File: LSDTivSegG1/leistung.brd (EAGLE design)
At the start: 150 x 100 mm, 87 parts, among them IC10 LM 2576 T15, IC11 LM 2576 T5.0, IC2 IR2184D, IC3 IR2184D, IC4 4081N, IC5 4069N, IC7 IR2184D, IC8 IR2184D, IC9 TINY13-20PU, Q1 IRFB3077, Q10 IRFB3077, Q11 IRFB3077, Q12 IRFB3077, Q2 IRFB3077, Q3 IRFB3077, Q4 IRFB3077, Q9 IRFB3077, X1 057-010-1, X2 MKDSN1,5/2-5,08

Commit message: added Text
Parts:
- F1, F2, F3: value (none) -> 1A
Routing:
- net GND: track 193.0 -> 181.2 mm
- net MOTOR_L_+: track 132.1 -> 123.8 mm
- net MOTOR_R_+: track 132.4 -> 130.8 mm
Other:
- board text added: "LSD-GR1-LST-D-T"
- board text added: "LSD-GR1-REG-D-+"
- board text added: "LSD-GR1-REG-D-BSTOP"
- board text added: "LSD-GR1-REG-D-TStop"

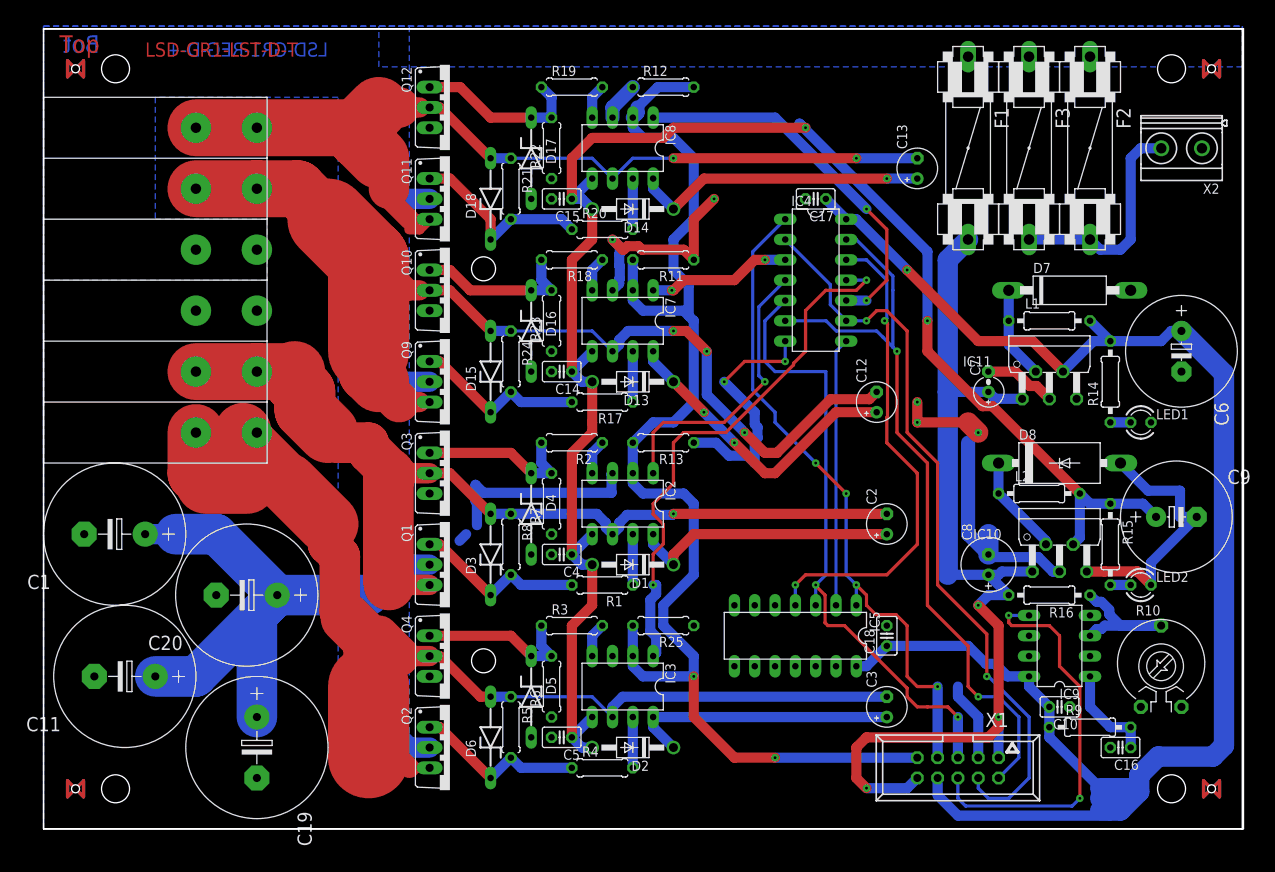
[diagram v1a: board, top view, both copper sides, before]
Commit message: fixes aus der Nachbesprechung
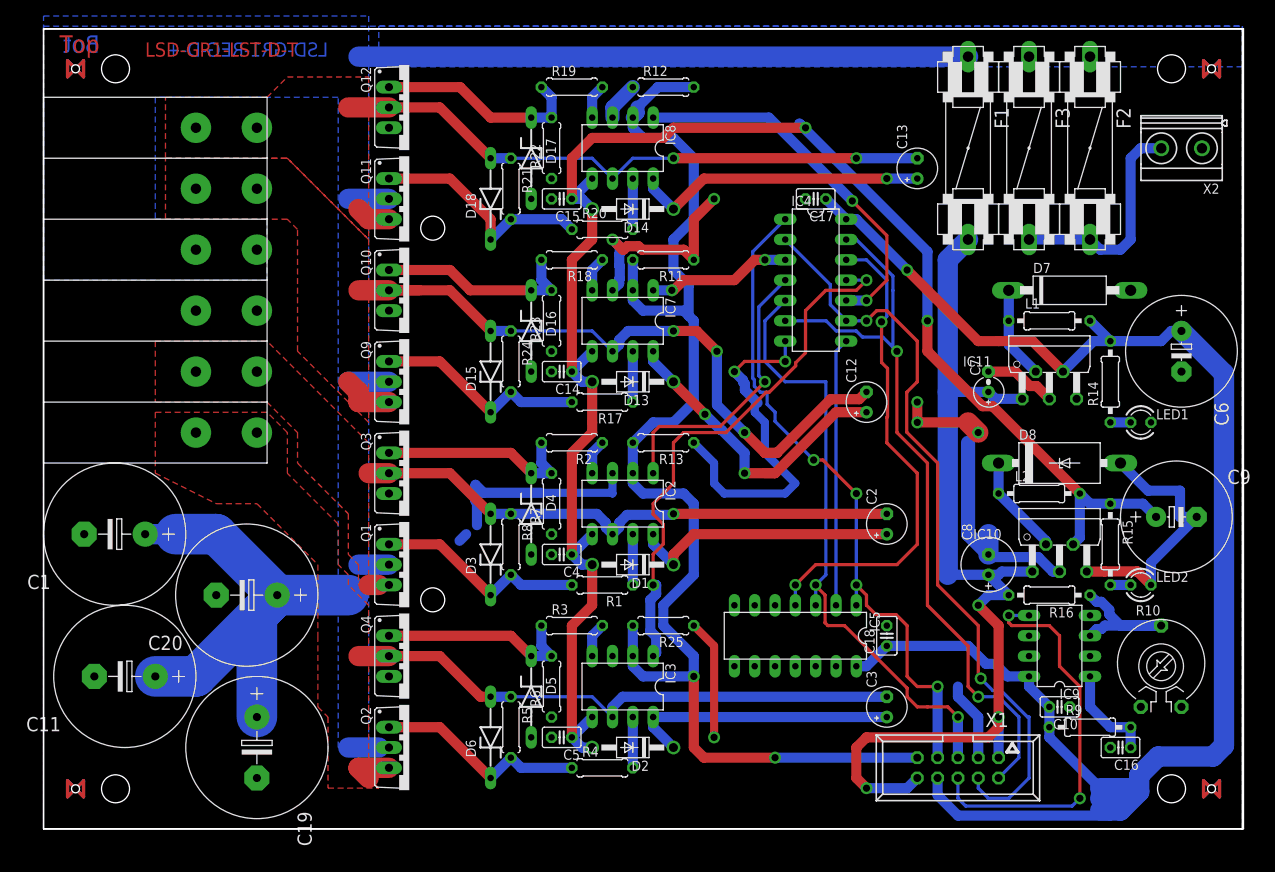
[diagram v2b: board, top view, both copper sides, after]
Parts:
- moved Q1 5.08 mm to (45.7, 33.0)
- moved Q10 5.08 mm to (45.7, 67.3)
- moved Q11 5.08 mm to (45.7, 78.7)
- moved Q12 5.08 mm to (45.7, 90.2)
- moved Q2 5.08 mm to (45.7, 10.2)
- moved Q3 5.08 mm to (45.7, 44.5)
- moved Q4 5.08 mm to (45.7, 21.6)
- moved Q9 5.08 mm to (45.7, 55.9)
- moved C12 1.27 mm to (102.9, 53.3)
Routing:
- net MOTOR_L_-: track 154.7 -> 76.6 mm
- net BAT_+: track 85.1 -> 159.5 mm
- net MOTOR_R_-: track 137.3 -> 84.0 mm
- net MOTOR_L_+: track 123.8 -> 72.2 mm
- net MOTOR_R_+: track 130.8 -> 94.9 mm
- net GND: track 181.2 -> 208.7 mm, vias 7 -> 8
- net N$8: track 20.6 -> 25.7 mm
- net N$7: track 22.0 -> 27.1 mm
- net N$6: track 22.0 -> 27.1 mm
- net N$5: track 20.6 -> 25.7 mm
- net N$32: track 21.2 -> 26.2 mm
- net N$31: track 24.0 -> 29.1 mm
- net N$30: track 22.0 -> 27.1 mm
- net N$13: track 20.6 -> 25.7 mm
- net ENABLE: track 162.1 -> 164.3 mm
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- added copper zone on layer 1, net MOTOR_L_+
- added copper zone on layer 1, net MOTOR_L_-
- added copper zone on layer 1, net MOTOR_R_+
- added copper zone on layer 1, net MOTOR_R_-
